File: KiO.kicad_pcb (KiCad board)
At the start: 2 copper layers, 56.5 x 50 mm, 9 parts, among them J2 LED RGB, J3 Moteur, U1 XIAO-ESP32-S3, U2 L293D, U3 Ultra Son HC-SR04, U4 Écran SSD 1306

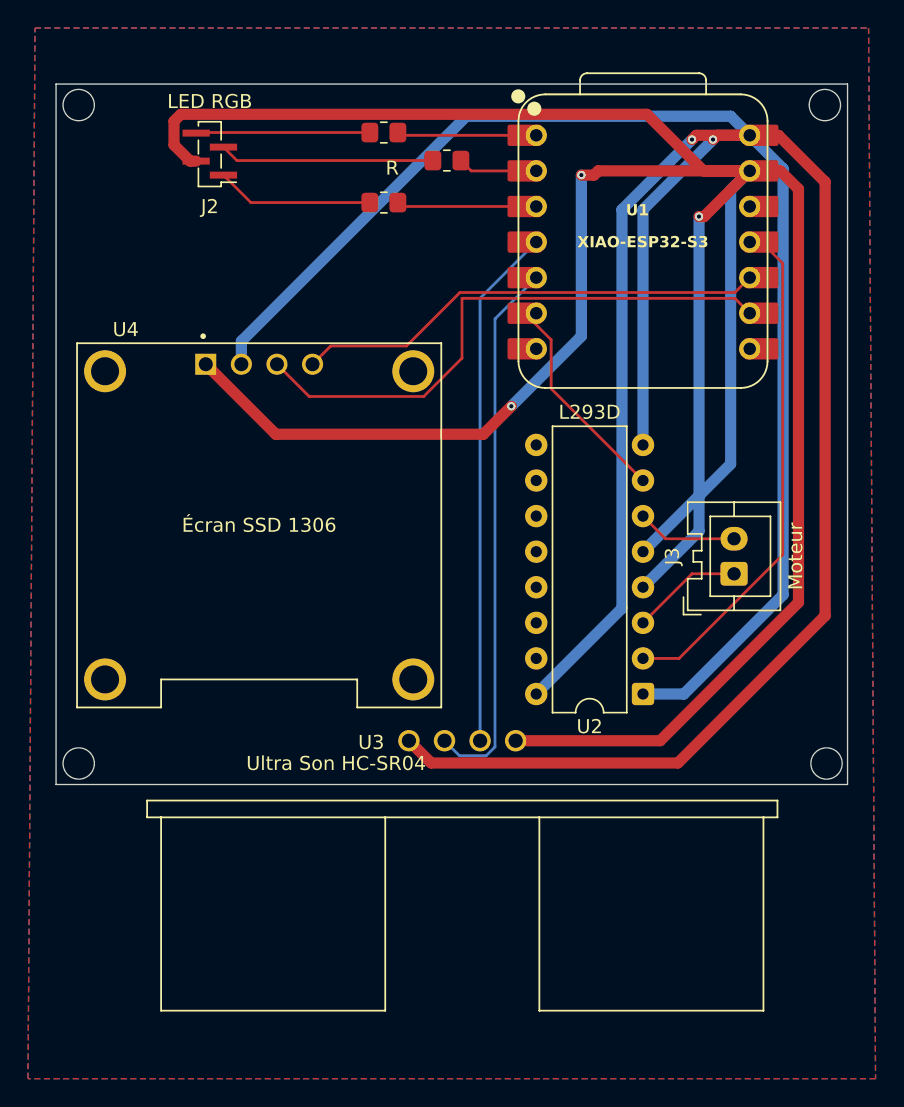
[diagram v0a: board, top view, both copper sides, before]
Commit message: fix screen display and connection
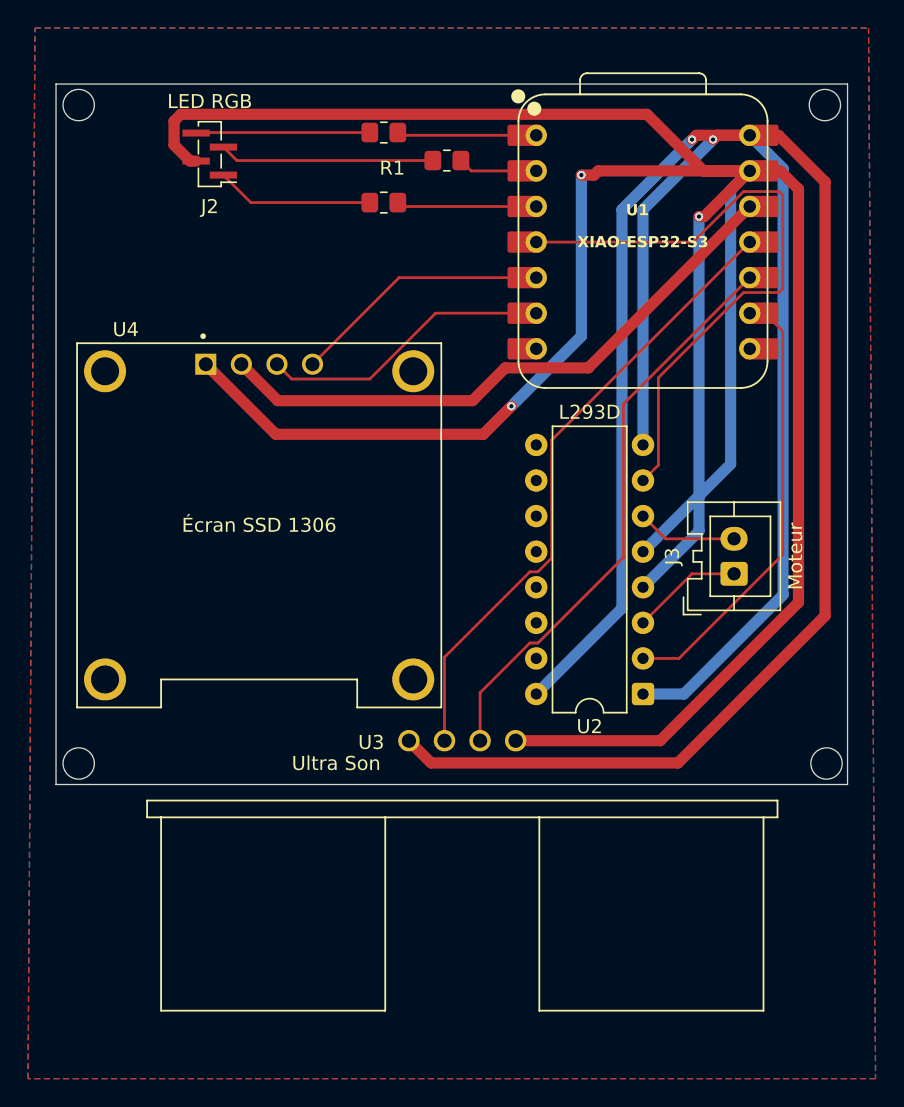
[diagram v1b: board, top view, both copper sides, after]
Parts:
- U3: value Ultra Son HC-SR04 -> Ultra Son
- renumbered R to R1
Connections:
- U1 pad 12: unconnected-(U1-VCC_3V3-Pad12)_1 -> +3.3V
- U2 pad 2: Net-(U1-GPIO9/D10/A10/MOSI) -> Net-(U1-GPIO7/D8/A8/SCK)
- U2 pad 7: Net-(U1-GPIO9/D5/I2C_SCL) -> Net-(U1-GPIO4/D3/A3)
- U3 pad 2: Net-(U1-GPIO5/D4/I2C_SDA) -> Net-(U1-GPIO9/D10/A10/MOSI)
- U3 pad 3: Net-(U1-GPIO4/D3/A3) -> Net-(U1-GPIO8/D9/A9/MISO)
- U4 pad 2: VCC -> +3.3V
- U4 pad 3: Net-(U1-GPIO7/D8/A8/SCK) -> Net-(U1-GPIO9/D5/I2C_SCL)
- U4 pad 4: Net-(U1-GPIO8/D9/A9/MISO) -> Net-(U1-GPIO5/D4/I2C_SDA)
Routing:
- net VCC: track 239.4 -> 194.2 mm
- net +3.3V: track 0.00 -> 43.1 mm
- net Net-(U1-GPIO5/D4/I2C_SDA): track 40.7 -> 18.5 mm
- net Net-(U1-GPIO9/D10/A10/MOSI): track 36.0 -> 45.0 mm
- net Net-(U1-GPIO4/D3/A3): track 37.3 -> 46.0 mm
- net Net-(U1-GPIO7/D8/A8/SCK): track 40.5 -> 31.9 mm
- net Net-(U1-GPIO8/D9/A9/MISO): track 33.8 -> 41.4 mm
- net Net-(U1-GPIO9/D5/I2C_SCL): track 15.4 -> 20.9 mm

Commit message: update
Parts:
- renumbered R1 to R
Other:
- board text added: "GND"
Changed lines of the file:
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@@
 		(descr "Resistor SMD 0805 (2012 Metric), square (rectangular) end terminal, IPC-7351 nominal with elongated pad for handsoldering. (Body size source: IPC-SM-782 page 72, https://www.pcb-3d.com/wordpress/wp-content/uploads/ipc-sm-782a_amendment_1_and_2.pdf), generated with kicad-footprint-generator")
 		(tags "resistor handsolder")
-		(property "Reference" "R1"
+		(property "Reference" "R"
 			(at -0.601 -2.5395 0)
 			(layer "F.SilkS")
@@
 		(layer "Edge.Cuts")
 	)
+	(gr_text "GND"
+		(at 111 54.5 0)
+		(layer "F.SilkS")
+		(effects
+			(font
+				(size 1 1)
+				(thickness 0.2)
+				(bold yes)
+			)
+			(justify left bottom)
+		)
+	)
 	(segment
